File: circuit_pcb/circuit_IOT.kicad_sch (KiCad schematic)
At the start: 13 parts, among them J1 TB007-508-02BE, J2 Conn_01x04, J4 UJ20-C-H-G-MSMT-4-P16-TR, U5 D3V3XA4B10LP

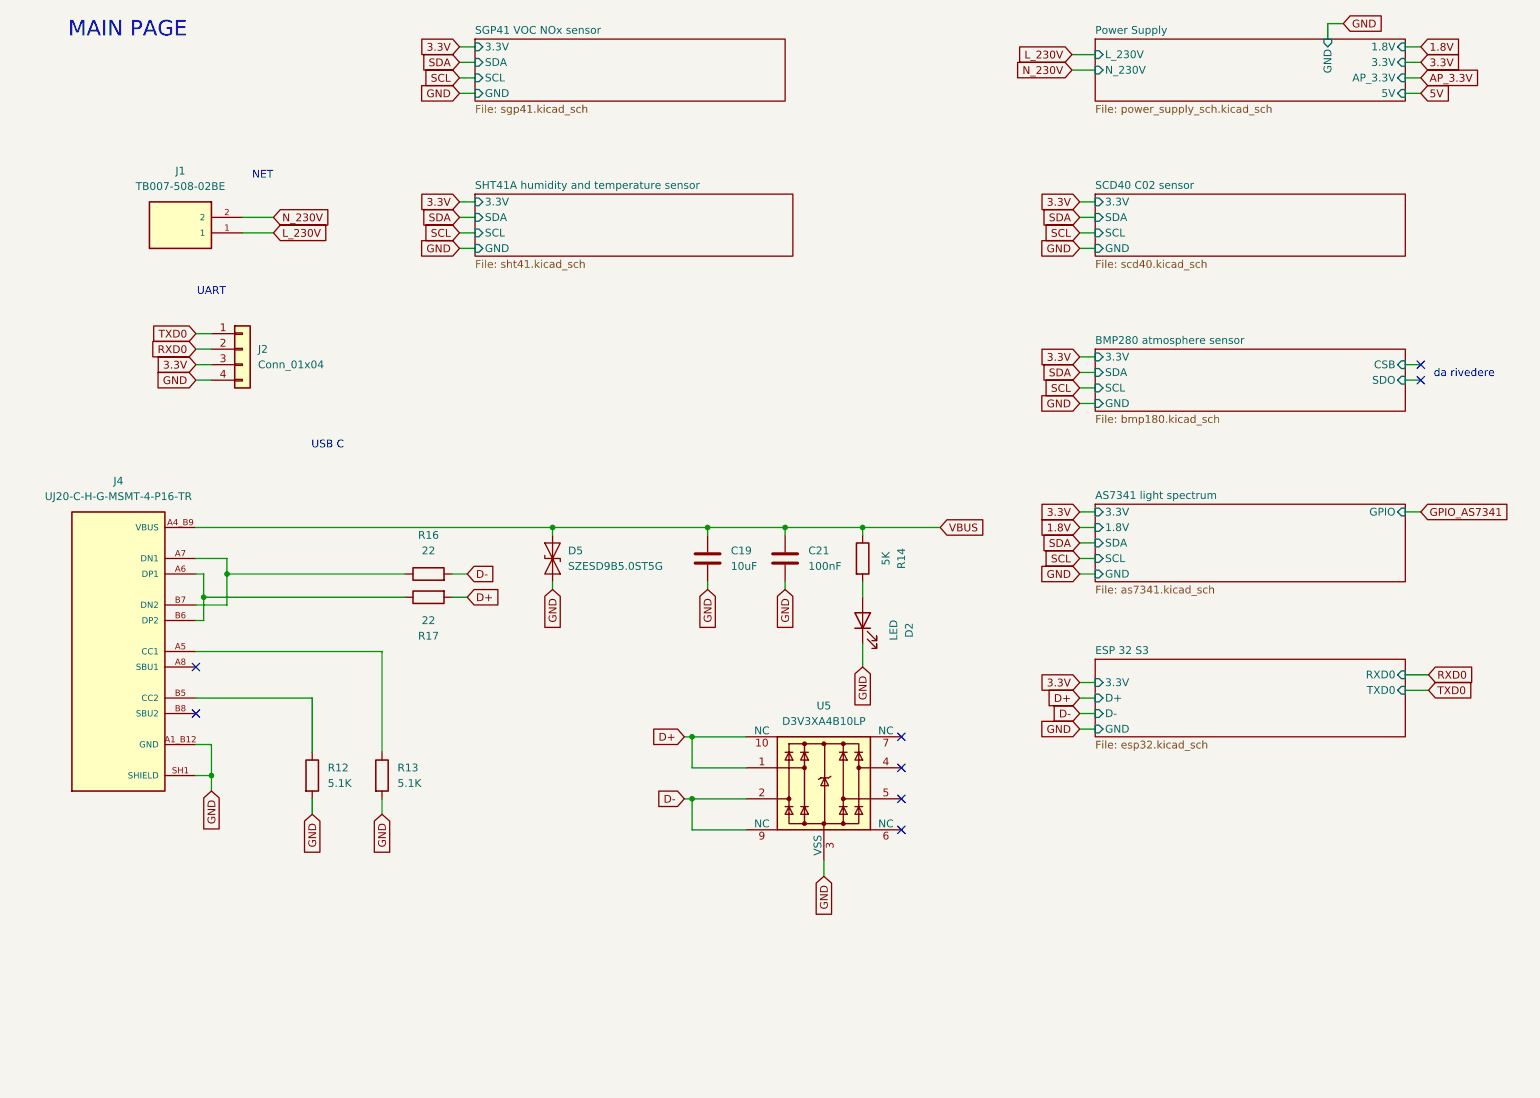
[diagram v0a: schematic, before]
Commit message: [new] circuit pcb: added PMS7003
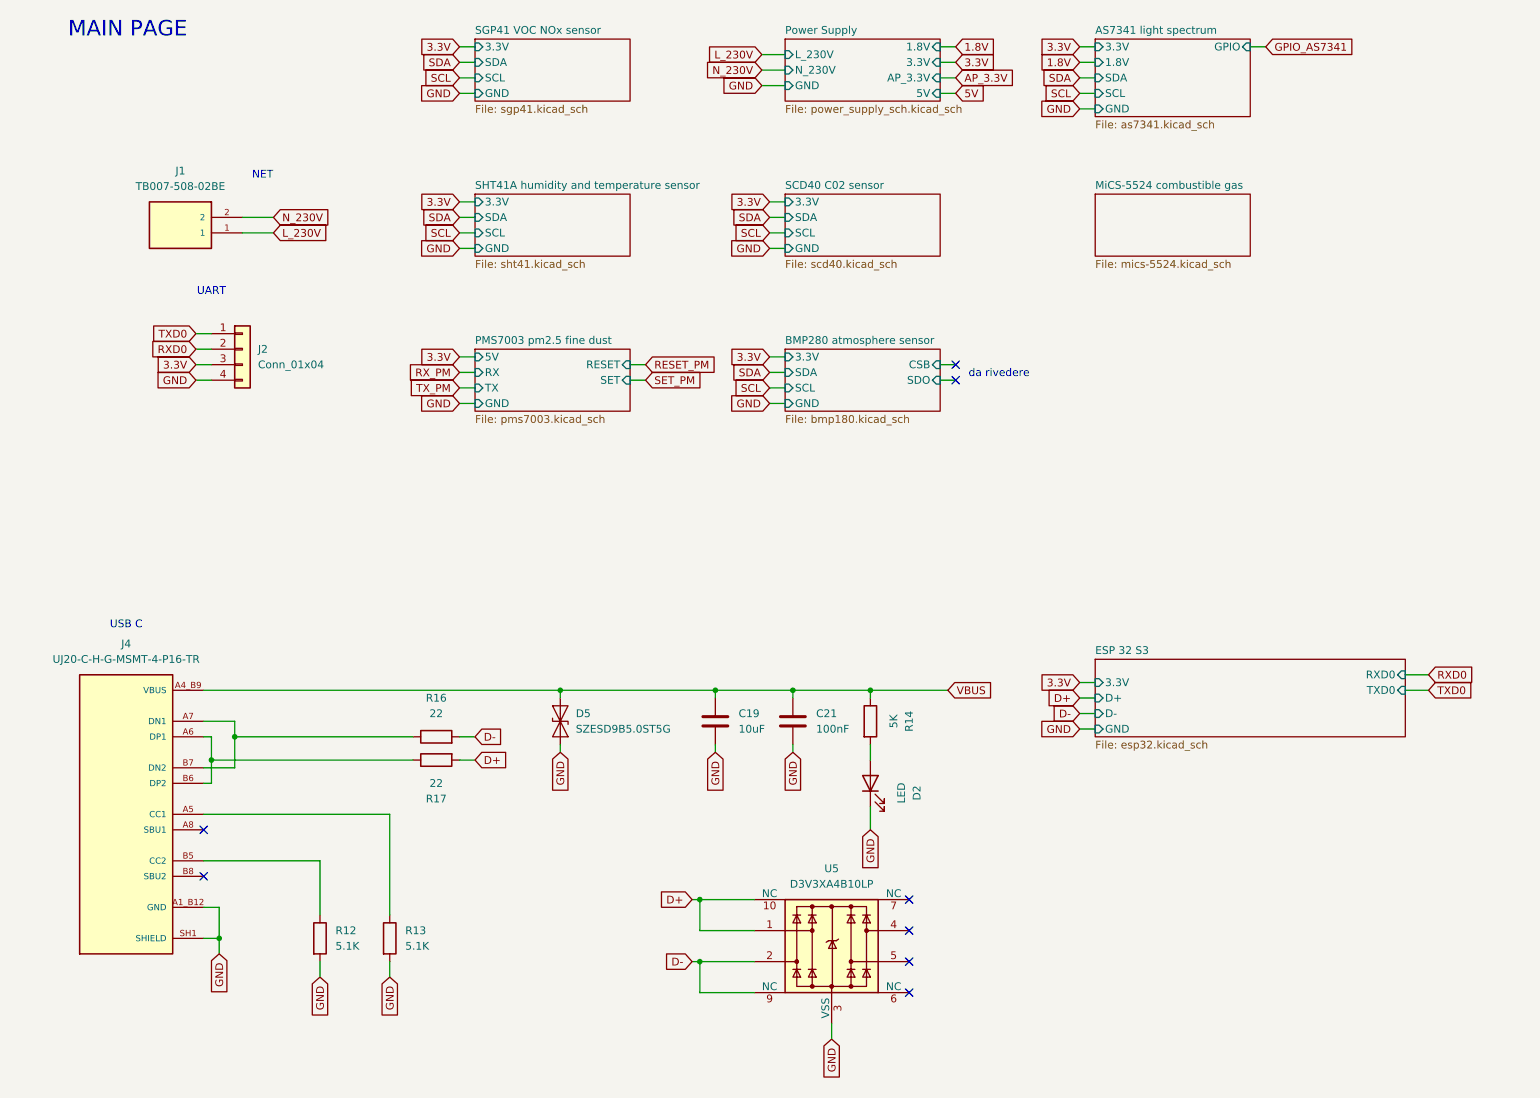
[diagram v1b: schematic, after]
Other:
- added sheet MiCS-5524 combustible gas (mics-5524.kicad_sch)
- added sheet PMS7003 pm2.5 fine dust (pms7003.kicad_sch)
- moved on the sheet: C19, C21, D2, D5, J4, R12, R13, R14, R16, R17, U5
